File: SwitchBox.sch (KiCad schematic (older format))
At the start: 64 parts

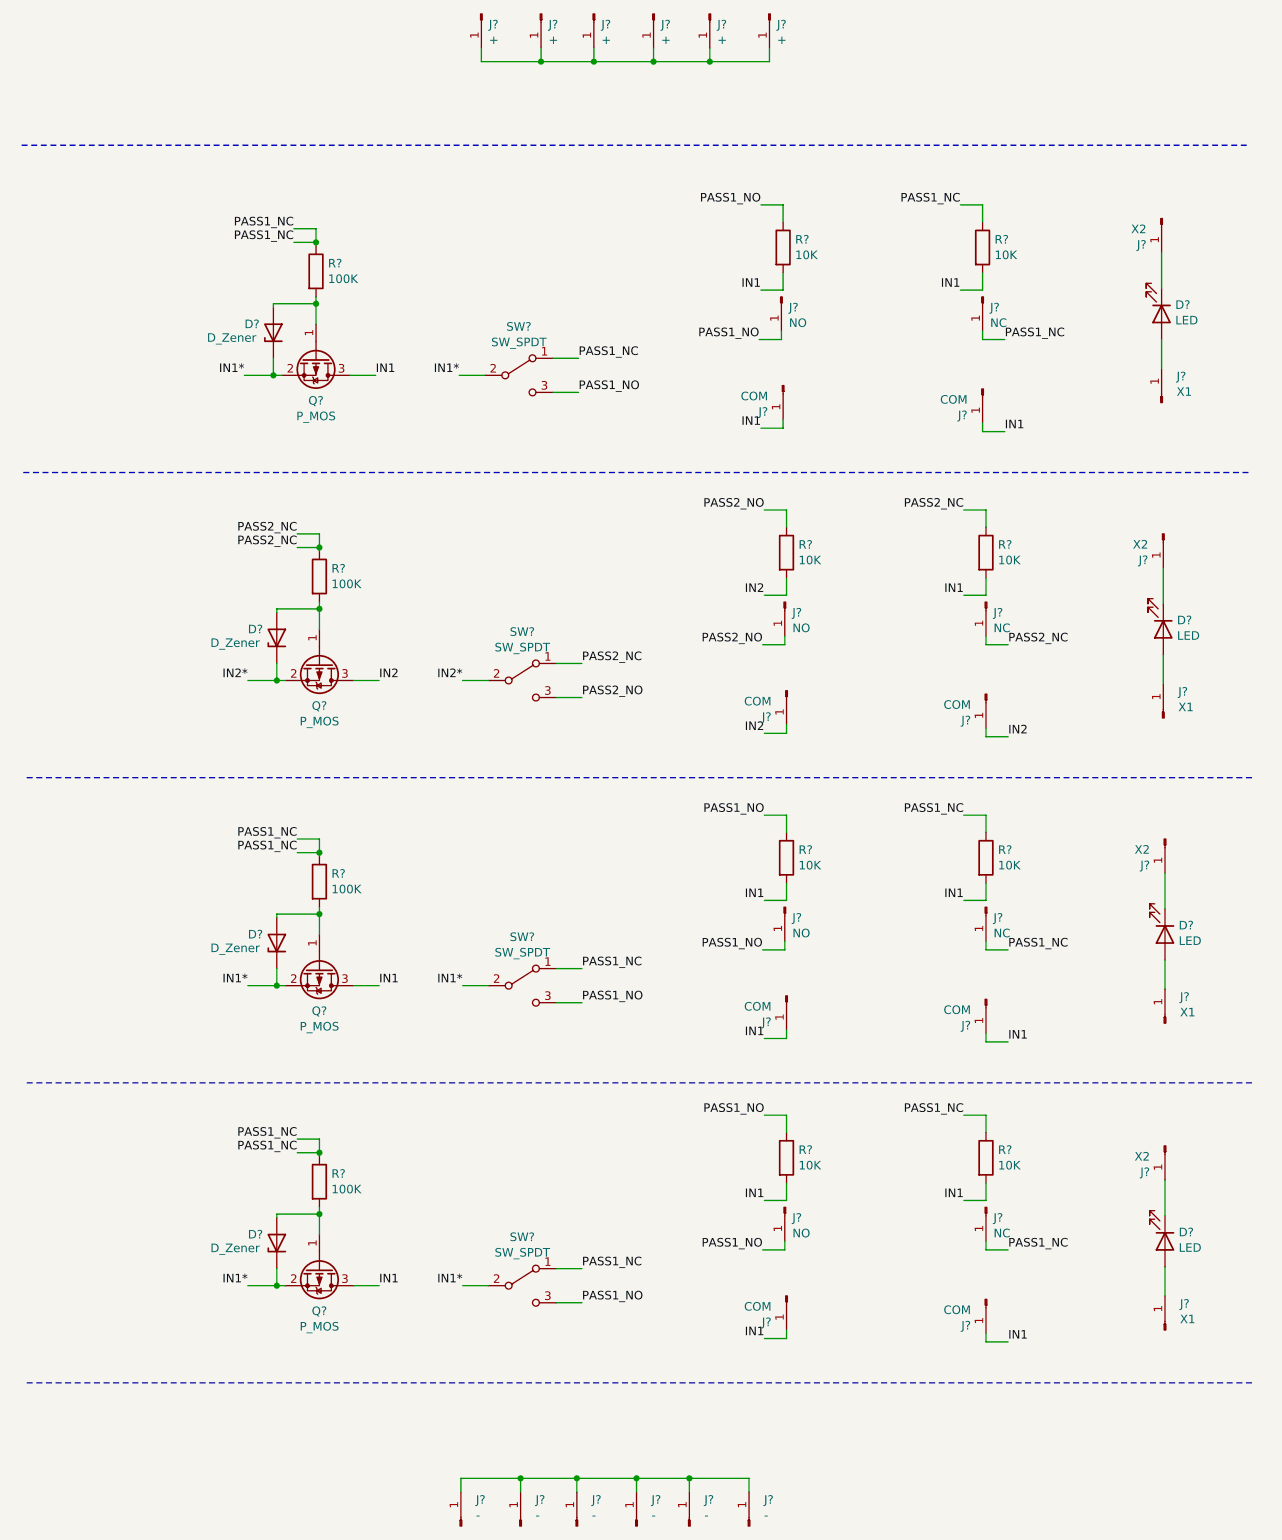
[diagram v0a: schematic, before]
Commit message: PCB & SCHEMATIC
PCB is done (still needs dimensional testing using the 3D printer), updated schematic.
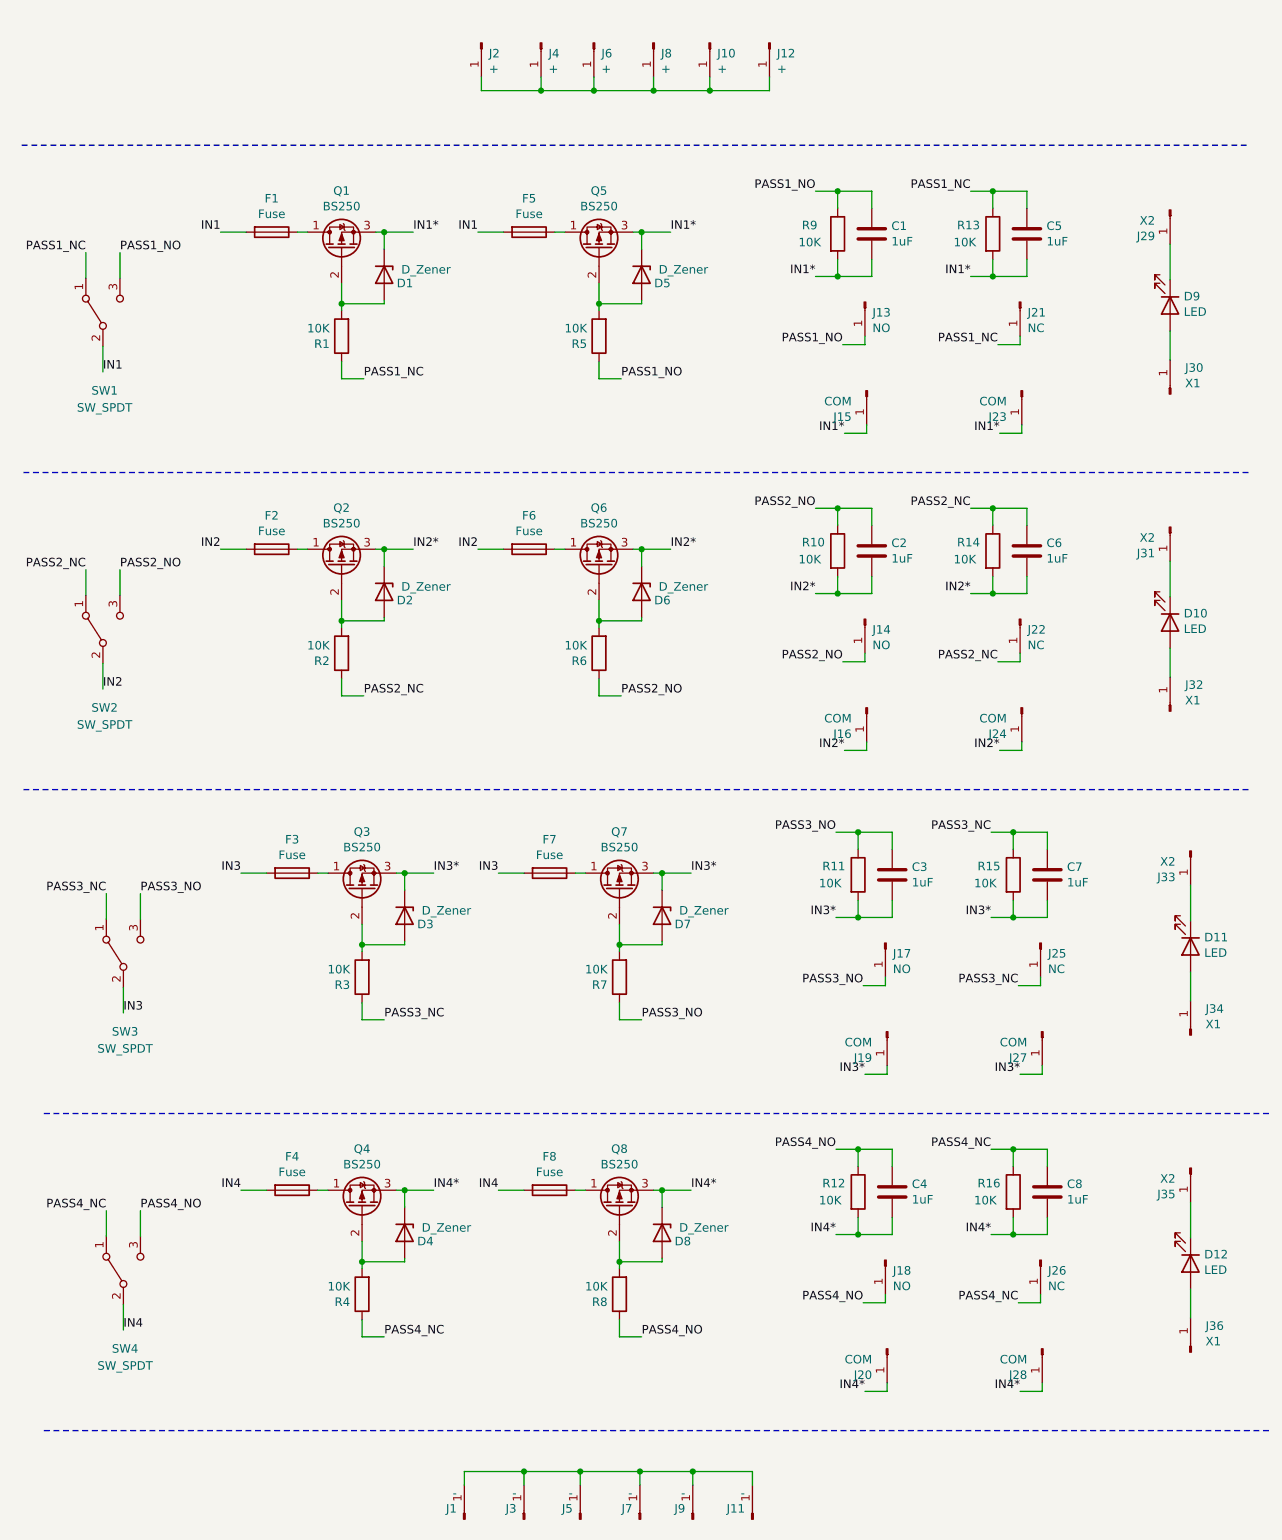
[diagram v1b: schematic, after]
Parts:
- removed D? (x3): D_Zener, symbol Device:D_Zener
- removed D? (x3): LED, symbol Device:LED
- removed J? (x7): COM, Connector:Banana_Jack_1Pin, symbol Connector:Conn_01x01_Male
- removed J? (x4): NC, Connector:Banana_Jack_1Pin, symbol Connector:Conn_01x01_Male
- removed J? (x6): -, Connector:Banana_Jack_1Pin, symbol Connector:Conn_01x01_Male
- removed J? (x3): NO, Connector:Banana_Jack_1Pin, symbol Connector:Conn_01x01_Male
- removed J? (x3): X2, Connector:Banana_Jack_1Pin, symbol Connector:Conn_01x01_Male
- removed J? (x3): X1, Connector:Banana_Jack_1Pin, symbol Connector:Conn_01x01_Male
- removed Q? (x4): P_MOS, Package_TO_SOT_SMD:TO-252-3_TabPin2, symbol Transistor_FET:FDN340P
- removed R? (x7): 10K, Resistor_SMD:R_1206_3216Metric, symbol Device:R
- removed R? (x3): 100K, Resistor_SMD:R_1206_3216Metric, symbol Device:R
- removed SW? (x3): SW_SPDT, symbol Switch:SW_SPDT
- added C1, C2, C3, C4, C5, C6, C7, C8: 1uF, Capacitor_SMD:C_1206_3216Metric_Pad1.33x1.80mm_HandSolder, symbol Device:C
- added D10, D11, D12: LED, additions:bulb, symbol Device:LED
- added D2, D3, D4, D5, D6, D7, D8: D_Zener, Diode_SMD:D_SOD-323, symbol Device:D_Zener
- added F1, F2, F3, F4, F5, F6, F7, F8: Fuse, Fuse:Fuse_2920_7451Metric, symbol Device:Fuse
- added J1, J11, J3, J5, J7, J9: -, additions:BananaPlug_custom, symbol Connector:Conn_01x01_Male
- added J14, J17, J18: NO, additions:BananaPlug_custom, symbol Connector:Conn_01x01_Male
- added J16, J19, J20, J23, J24, J27, J28: COM, additions:BananaPlug_custom, symbol Connector:Conn_01x01_Male
- added J21, J22, J25, J26: NC, additions:BananaPlug_custom, symbol Connector:Conn_01x01_Male
- added J31, J33, J35: X2, additions:BananaPlug_custom, symbol Connector:Conn_01x01_Male
- added J32, J34, J36: X1, additions:BananaPlug_custom, symbol Connector:Conn_01x01_Male
- added Q1, Q2, Q3, Q4, Q5, Q6, Q7, Q8: BS250, Package_TO_SOT_SMD:TO-252-3_TabPin2, symbol Transistor_FET:BS250
- added R10, R11, R12, R13, R14, R15, R16, R2, R3, R4, R5, R6, R7, R8: 10K, Resistor_SMD:R_1206_3216Metric, symbol Device:R
- added SW2, SW3, SW4: SW_SPDT, additions:switch, symbol Switch:SW_SPDT
- D1: renamed from D?; footprint (none) -> Diode_SMD:D_SOD-323
- D9: renamed from D?; footprint (none) -> additions:bulb
- J10, J12, J13, J15, J2, J29, J30, J4, J6, J8: renamed from J?; footprint Connector:Banana_Jack_1Pin -> additions:BananaPlug_custom
- R1: renamed from R?; value 100K -> 10K
- SW1: renamed from SW?; footprint (none) -> additions:switch
- gave numbers to parts that had none: 1
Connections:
- net IN1: now also SW1.2 (B), F1.2, F5.2; no longer J15.1 (Pin_1), R9.2
- net IN1*: now also J15.1 (Pin_1), R9.2, C1.2, C5.2, D5.1 (K), J23.1 (Pin_1), Q1.3 (S), Q5.3 (S), R13.2; no longer SW1.2 (B)
- net IN2: now also F2.2, F6.2, SW2.2 (B)
- net IN2*: now also C2.2, C6.2, D2.1 (K), D6.1 (K), J16.1 (Pin_1), J24.1 (Pin_1), Q2.3 (S), Q6.3 (S), R10.2, R14.2
- net PASS1_NC: now also C5.1, J21.1 (Pin_1), R13.1
- net PASS1_NO: now also C1.1, R5.1
- net PASS2_NC: now also C6.1, J22.1 (Pin_1), R14.1, R2.1, SW2.1 (A)
- net PASS2_NO: now also C2.1, J14.1 (Pin_1), R10.1, R6.1, SW2.3 (C)
- net at D1.2 (A), R1.2: now also Q1.2 (G)
- new net: F1.1, Q1.1 (D)
- new net: D5.2 (A), Q5.2 (G), R5.2
- new net: F5.1, Q5.1 (D)
- new net: J1.1 (Pin_1), J11.1 (Pin_1), J3.1 (Pin_1), J5.1 (Pin_1), J7.1 (Pin_1), J9.1 (Pin_1)
- new net: D2.2 (A), Q2.2 (G), R2.2
- new net: D10.1 (K), J31.1 (Pin_1)
- new net: D10.2 (A), J32.1 (Pin_1)
- new net: F2.1, Q2.1 (D)
- new net: D6.2 (A), Q6.2 (G), R6.2
- new net: F6.1, Q6.1 (D)
- new net: D3.2 (A), Q3.2 (G), R3.2
- new net: D11.1 (K), J33.1 (Pin_1)
- new net: D11.2 (A), J34.1 (Pin_1)
- new net: F3.1, Q3.1 (D)
- new net: D7.2 (A), Q7.2 (G), R7.2
- new net: F7.1, Q7.1 (D)
- new net: D4.2 (A), Q4.2 (G), R4.2
- new net: D12.1 (K), J35.1 (Pin_1)
- new net: D12.2 (A), J36.1 (Pin_1)
- new net: F4.1, Q4.1 (D)
- new net: D8.2 (A), Q8.2 (G), R8.2
- new net: F8.1, Q8.1 (D)
- new net IN3: F3.2, F7.2, SW3.2 (B)
- new net IN3*: C3.2, C7.2, D3.1 (K), D7.1 (K), J19.1 (Pin_1), J27.1 (Pin_1), Q3.3 (S), Q7.3 (S), R11.2, R15.2
- new net IN4: F4.2, F8.2, SW4.2 (B)
- new net IN4*: C4.2, C8.2, D4.1 (K), D8.1 (K), J20.1 (Pin_1), J28.1 (Pin_1), Q4.3 (S), Q8.3 (S), R12.2, R16.2
- new net PASS3_NC: C7.1, J25.1 (Pin_1), R15.1, R3.1, SW3.1 (A)
- new net PASS3_NO: C3.1, J17.1 (Pin_1), R11.1, R7.1, SW3.3 (C)
- new net PASS4_NC: C8.1, J26.1 (Pin_1), R16.1, R4.1, SW4.1 (A)
- new net PASS4_NO: C4.1, J18.1 (Pin_1), R12.1, R8.1, SW4.3 (C)
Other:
- moved on the sheet: D1, D9, J10, J12, J13, J15, J2, J29, J30, J4, J6, J8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
